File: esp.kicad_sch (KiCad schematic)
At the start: 31 parts, among them J401 57PC5F, J402 57PC5F, J403 I2S, Q401 MMBT3904, U401 ESP32-DEVKITC-VE, U402 6N138

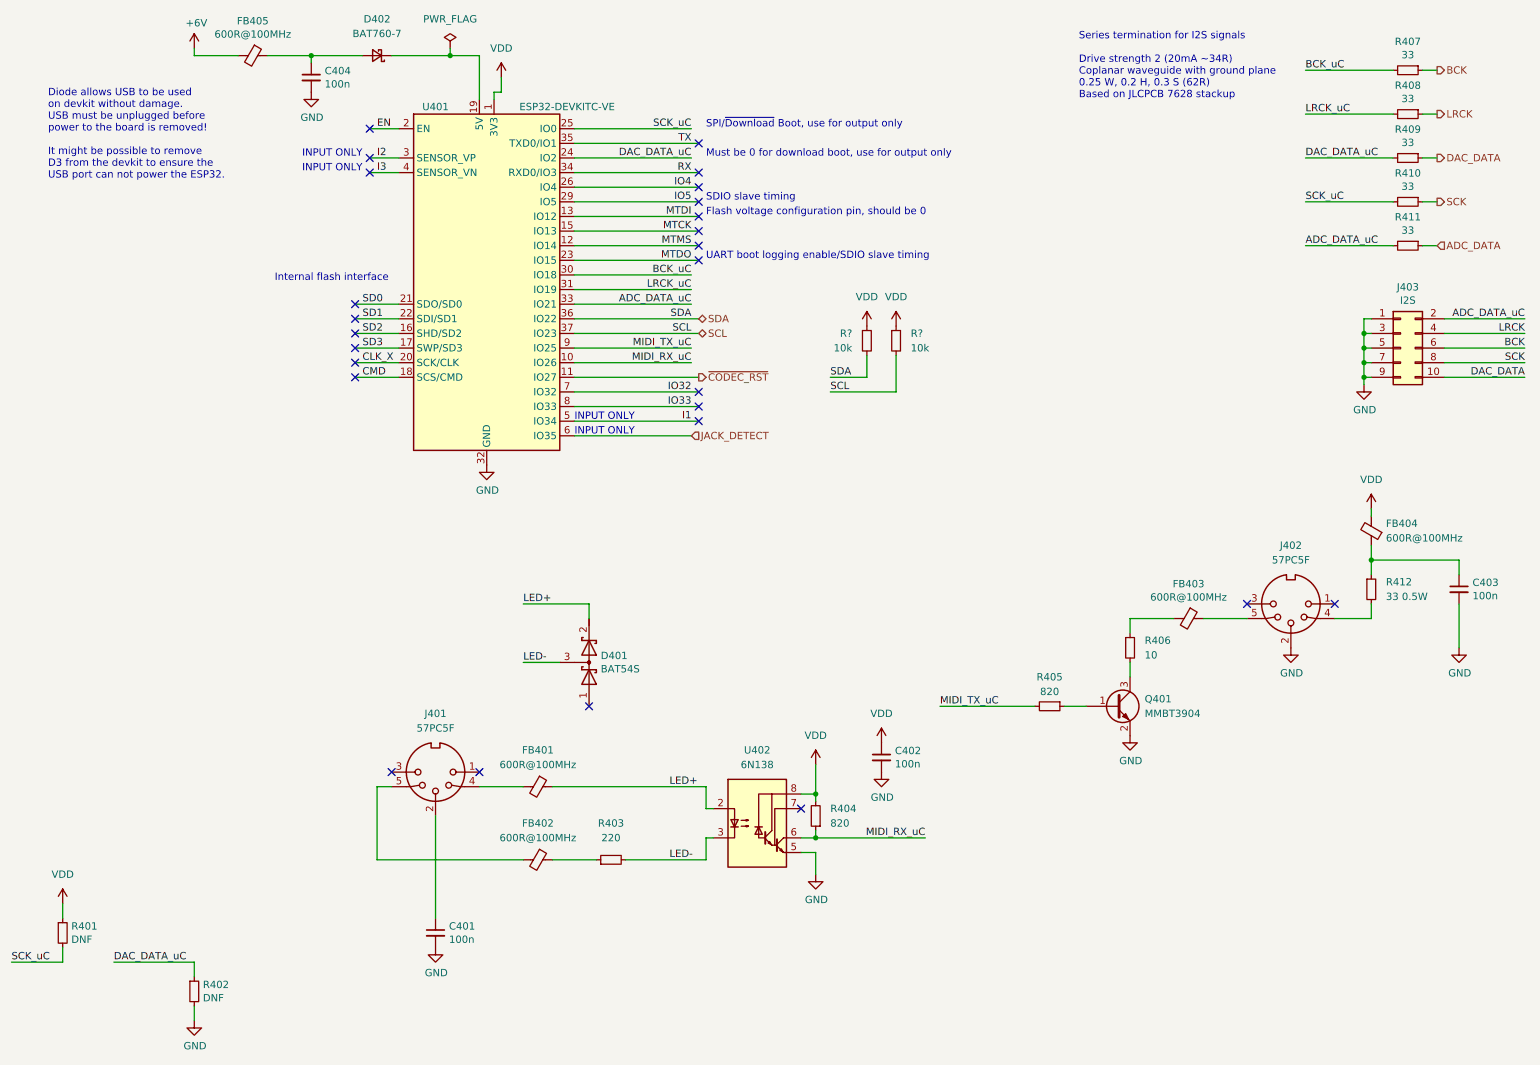
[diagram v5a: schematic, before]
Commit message: Update some part numbers for in-stock parts
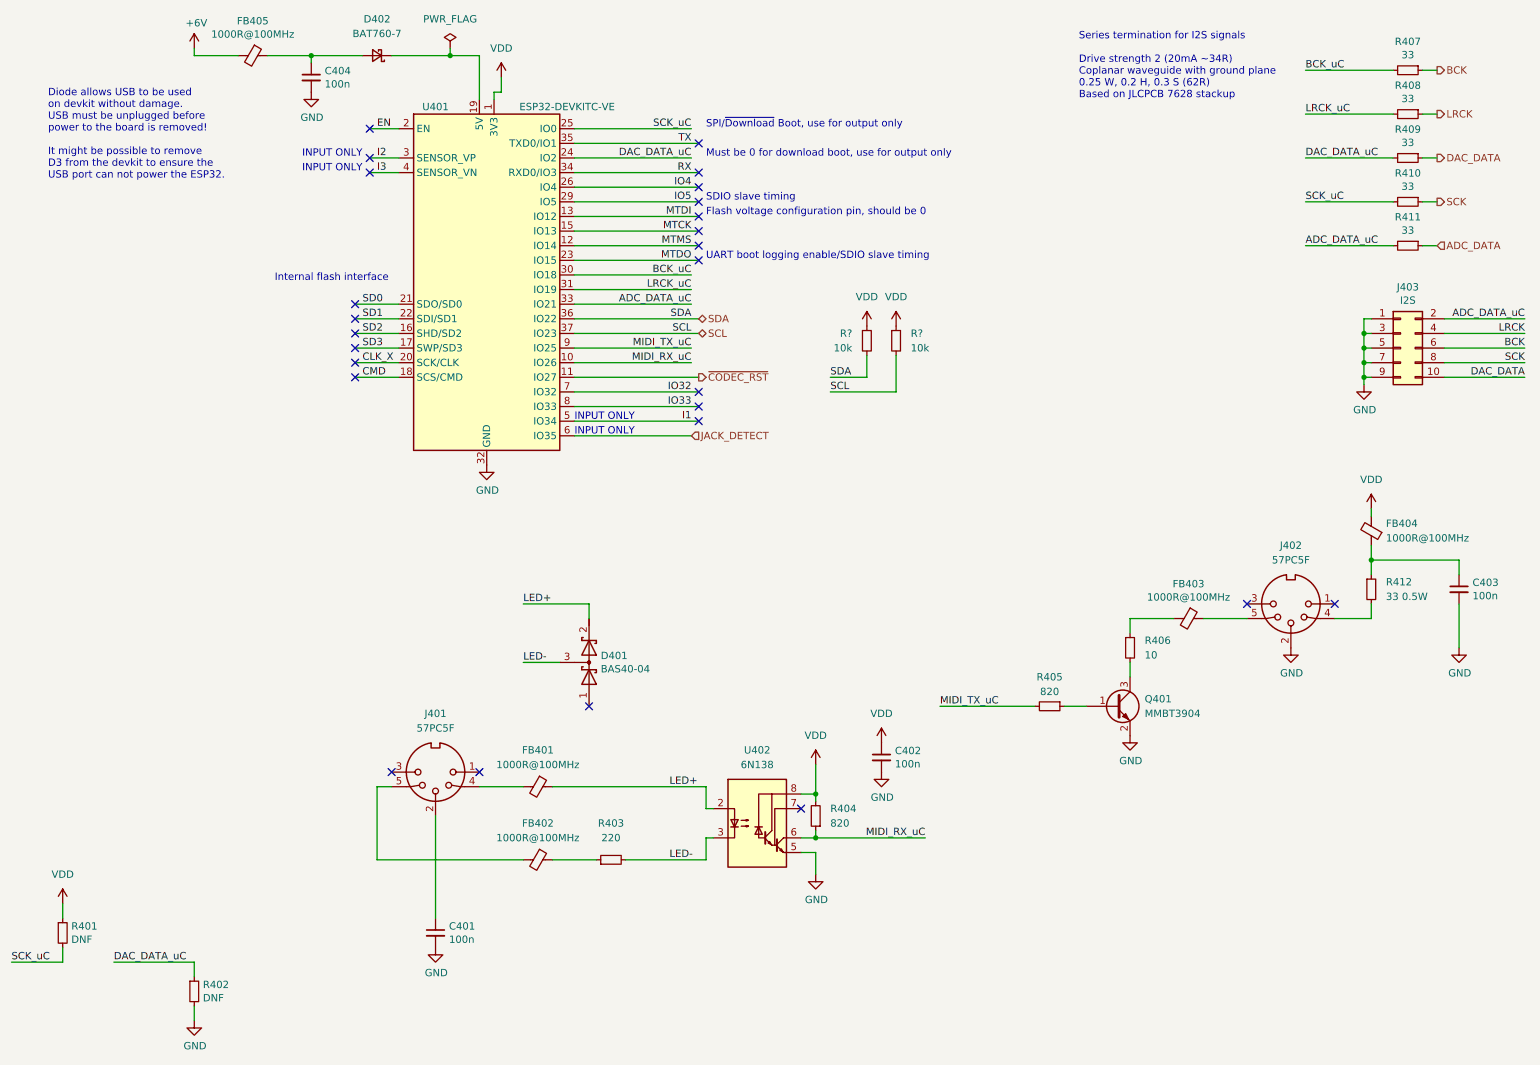
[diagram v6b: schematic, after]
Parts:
- D401: value BAT54S -> BAS40-04; PN BAT54S -> BAS40-04,235
- FB401, FB402, FB403, FB404, FB405: value 600R@100MHz -> 1000R@100MHz; PN BLM21SP601SN1 -> 2508051027Y1
- R406: PN CR0805-FX-10R0ELF -> CR0805AFX-10R0EAS
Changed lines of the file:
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@@
       (effects (font (size 1.27 1.27)) hide)
     )
-    (property "PN" "CR0805-FX-10R0ELF" (id 4) (at 212.09 123.19 0)
+    (property "PN" "CR0805AFX-10R0EAS" (id 4) (at 212.09 123.19 0)
       (effects (font (size 1.27 1.27)) hide)
     )
@@
     (in_bom yes) (on_board yes)
     (property "Reference" "FB405" (id 0) (at 59.69 14.3002 90))
-    (property "Value" "600R@100MHz" (id 1) (at 59.69 16.6116 90))
+    (property "Value" "1000R@100MHz" (id 1) (at 59.69 16.6116 90))
     (property "Footprint" "Resistor_SMD:R_0805_2012Metric_Pad1.20x1.40mm_HandSolder" (id 2) (at 59.69 18.542 90)
       (effects (font (size 1.27 1.27)) hide)
     )
-    (property "Datasheet" "~" (id 3) (at 59.69 20.32 0)
-      (effects (font (size 1.27 1.27)) hide)
-    )
-    (property "PN" "BLM21SP601SN1" (id 4) (at 59.69 20.32 0)
+    (property "Datasheet" "https://www.mouser.co.uk/datasheet/2/150/2508051027Y1-1511733.pdf" (id 3) (at 59.69 20.32 0)
+      (effects (font (size 1.27 1.27)) hide)
+    )
+    (property "PN" "2508051027Y1" (id 4) (at 59.69 20.32 0)
       (effects (font (size 1.27 1.27)) hide)
     )
@@
     (in_bom yes) (on_board yes) (fields_autoplaced)
     (property "Reference" "FB401" (id 0) (at 109.22 140.97 90))
-    (property "Value" "600R@100MHz" (id 1) (at 109.22 143.51 90))
+    (property "Value" "1000R@100MHz" (id 1) (at 109.22 143.51 90))
     (property "Footprint" "Resistor_SMD:R_0805_2012Metric_Pad1.20x1.40mm_HandSolder" (id 2) (at 109.22 145.542 90)
       (effects (font (size 1.27 1.27)) hide)
     )
-    (property "Datasheet" "~" (id 3) (at 109.22 147.32 0)
-      (effects (font (size 1.27 1.27)) hide)
-    )
-    (property "PN" "BLM21SP601SN1" (id 4) (at 109.22 147.32 0)
+    (property "Datasheet" "https://www.mouser.co.uk/datasheet/2/150/2508051027Y1-1511733.pdf" (id 3) (at 109.22 147.32 0)
+      (effects (font (size 1.27 1.27)) hide)
+    )
+    (property "PN" "2508051027Y1" (id 4) (at 109.22 147.32 0)
       (effects (font (size 1.27 1.27)) hide)
     )
@@
     (in_bom yes) (on_board yes) (fields_autoplaced)
     (property "Reference" "FB402" (id 0) (at 109.22 153.67 90))
-    (property "Value" "600R@100MHz" (id 1) (at 109.22 156.21 90))
+    (property "Value" "1000R@100MHz" (id 1) (at 109.22 156.21 90))
     (property "Footprint" "Resistor_SMD:R_0805_2012Metric_Pad1.20x1.40mm_HandSolder" (id 2) (at 109.22 158.242 90)
       (effects (font (size 1.27 1.27)) hide)
     )
-    (property "Datasheet" "~" (id 3) (at 109.22 160.02 0)
-      (effects (font (size 1.27 1.27)) hide)
-    )
-    (property "PN" "BLM21SP601SN1" (id 4) (at 109.22 160.02 0)
+    (property "Datasheet" "https://www.mouser.co.uk/datasheet/2/150/2508051027Y1-1511733.pdf" (id 3) (at 109.22 160.02 0)
+      (effects (font (size 1.27 1.27)) hide)
+    )
+    (property "PN" "2508051027Y1" (id 4) (at 109.22 160.02 0)
       (effects (font (size 1.27 1.27)) hide)
     )
@@
     (in_bom yes) (on_board yes)
     (property "Reference" "FB403" (id 0) (at 222.25 112.0902 90))
-    (property "Value" "600R@100MHz" (id 1) (at 222.25 114.4016 90))
+    (property "Value" "1000R@100MHz" (id 1) (at 222.25 114.4016 90))
     (property "Footprint" "Resistor_SMD:R_0805_2012Metric_Pad1.20x1.40mm_HandSolder" (id 2) (at 222.25 116.332 90)
       (effects (font (size 1.27 1.27)) hide)
     )
-    (property "Datasheet" "~" (id 3) (at 222.25 118.11 0)
-      (effects (font (size 1.27 1.27)) hide)
-    )
-    (property "PN" "BLM21SP601SN1" (id 4) (at 222.25 118.11 0)
+    (property "Datasheet" "https://www.mouser.co.uk/datasheet/2/150/2508051027Y1-1511733.pdf" (id 3) (at 222.25 118.11 0)
+      (effects (font (size 1.27 1.27)) hide)
+    )
+    (property "PN" "2508051027Y1" (id 4) (at 222.25 118.11 0)
       (effects (font (size 1.27 1.27)) hide)
     )
@@
       (effects (font (size 1.27 1.27)) (justify right))
     )
-    (property "Value" "600R@100MHz" (id 1) (at 256.54 104.1399 0)
+    (property "Value" "1000R@100MHz" (id 1) (at 256.54 104.1399 0)
       (effects (font (size 1.27 1.27)) (justify right))
     )
@@
       (effects (font (size 1.27 1.27)) hide)
     )
-    (property "Datasheet" "~" (id 3) (at 254 102.87 0)
-      (effects (font (size 1.27 1.27)) hide)
-    )
-    (property "PN" "BLM21SP601SN1" (id 4) (at 254 102.87 0)
+    (property "Datasheet" "https://www.mouser.co.uk/datasheet/2/150/2508051027Y1-1511733.pdf" (id 3) (at 254 102.87 0)
+      (effects (font (size 1.27 1.27)) hide)
+    )
+    (property "PN" "2508051027Y1" (id 4) (at 254 102.87 0)
       (effects (font (size 1.27 1.27)) hide)
     )
@@
       (effects (font (size 1.27 1.27)) (justify left))
     )
-    (property "Value" "BAT54S" (id 1) (at 120.142 126.873 90)
+    (property "Value" "BAS40-04" (id 1) (at 120.142 126.873 90)
       (effects (font (size 1.27 1.27)) (justify left))
     )
@@
       (effects (font (size 1.27 1.27)) hide)
     )
-    (property "Datasheet" "~" (id 3) (at 118.11 125.73 0)
-      (effects (font (size 1.27 1.27)) hide)
-    )
-    (property "PN" "BAT54S" (id 4) (at 118.11 125.73 0)
-      (effects (font (size 1.27 1.27)) hide)
-    )
+    (property "Datasheet" "https://www.mouser.co.uk/datasheet/2/916/BAS40_1PSXXSB4X_SER-1598244.pdf" (id 3) (at 118.11 125.73 0)
+      (effects (font (size 1.27 1.27)) hide)
+    )
+    (property "PN" "BAS40-04,235" (id 4) (at 118.11 125.73 0)
+      (effects (font (size 1.27 1.27)) hide)
+    )

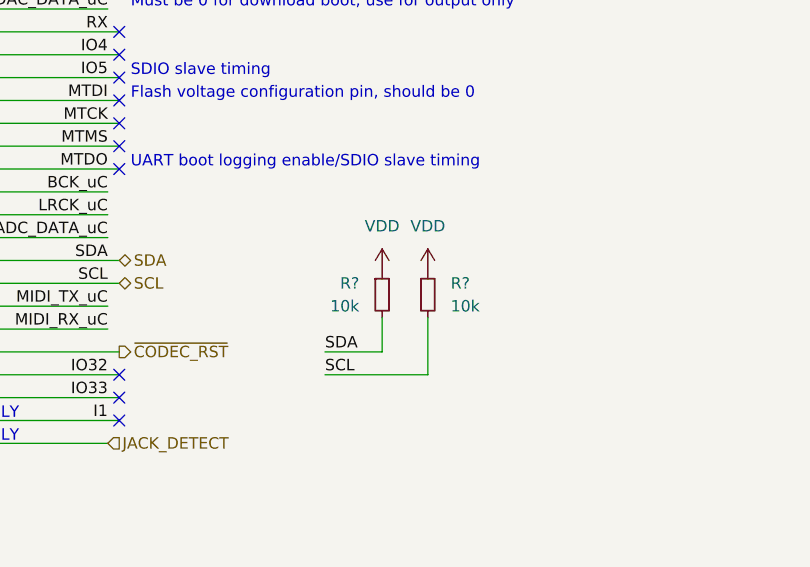
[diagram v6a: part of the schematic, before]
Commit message: Add new switchmode power supply
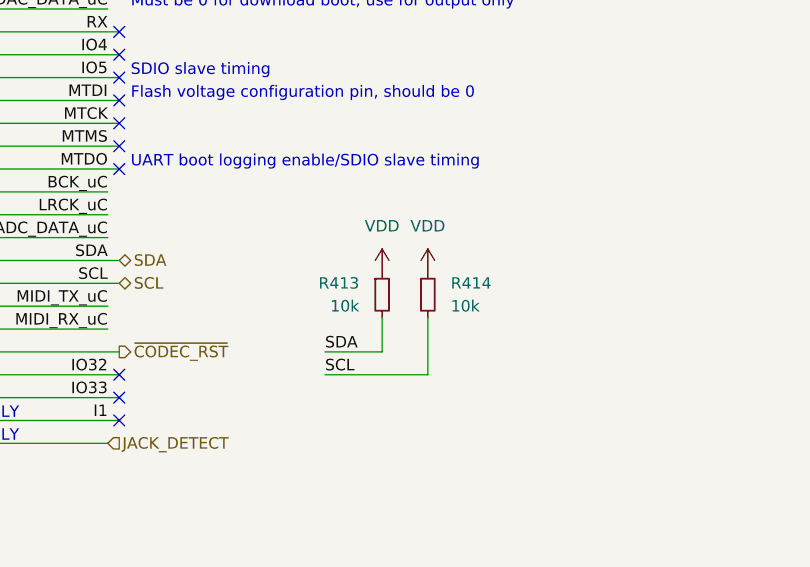
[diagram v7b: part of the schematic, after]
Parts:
- gave numbers to parts that had none: 2
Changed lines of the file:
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@@
   (symbol (lib_id "power:VDD") (at 166.37 67.31 0) (unit 1)
     (in_bom yes) (on_board yes) (fields_autoplaced)
-    (property "Reference" "#PWR?" (id 0) (at 166.37 71.12 0)
+    (property "Reference" "#PWR0416" (id 0) (at 166.37 71.12 0)
       (effects (font (size 1.27 1.27)) hide)
     )
@@
   (symbol (lib_id "power:VDD") (at 171.45 67.31 0) (unit 1)
     (in_bom yes) (on_board yes) (fields_autoplaced)
-    (property "Reference" "#PWR?" (id 0) (at 171.45 71.12 0)
+    (property "Reference" "#PWR0417" (id 0) (at 171.45 71.12 0)
       (effects (font (size 1.27 1.27)) hide)
     )
@@
   (symbol (lib_id "Device:R_Small") (at 166.37 69.85 0) (unit 1)
     (in_bom yes) (on_board yes) (fields_autoplaced)
-    (property "Reference" "R?" (id 0) (at 163.83 68.5799 0)
+    (property "Reference" "R413" (id 0) (at 163.83 68.5799 0)
       (effects (font (size 1.27 1.27)) (justify right))
     )
@@
   (symbol (lib_id "Device:R_Small") (at 171.45 69.85 0) (unit 1)
     (in_bom yes) (on_board yes) (fields_autoplaced)
-    (property "Reference" "R?" (id 0) (at 173.99 68.5799 0)
-      (effects (font (size 1.27 1.27)) (justify left))
-    )
+    (property "Reference" "R414" (id 0) (at 173.99 68.5799 0)
+      (effects (font (size 1.27 1.27)) (justify left))
+    )
